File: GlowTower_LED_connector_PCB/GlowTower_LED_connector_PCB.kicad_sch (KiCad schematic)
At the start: 7 parts, among them SW1 TS-1102S-C-A-B, U1 LED strip, U2 LED strip, U3 LED strip, U4 LED strip, U5 SMTSO3015CTJ, U6 SMTSO3015CTJ

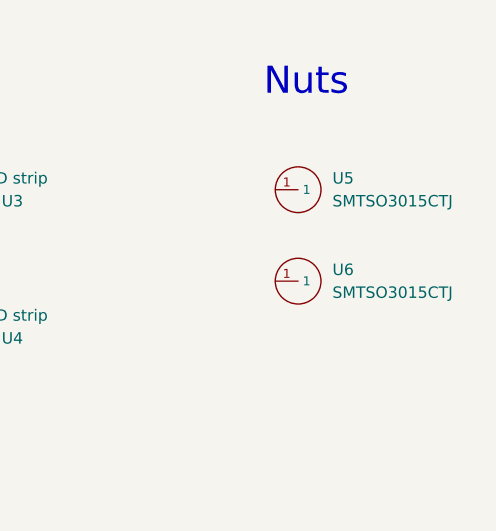
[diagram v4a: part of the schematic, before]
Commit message: improved connection to top case, added new glowtower design
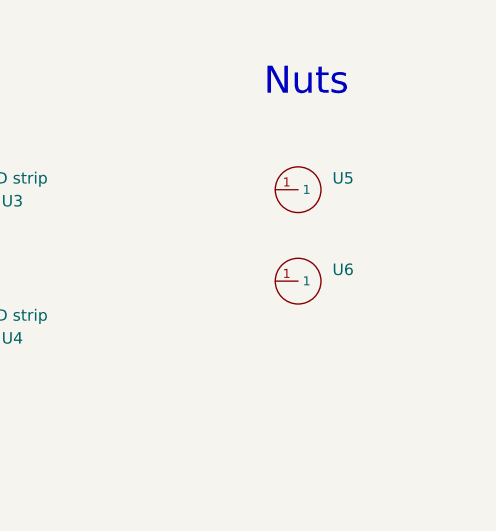
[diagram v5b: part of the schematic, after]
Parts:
- U5, U6: value SMTSO3015CTJ -> (none); footprint footprint:SMTSO3030CTJ -> (none); now left out of the parts list
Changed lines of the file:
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@@
   )
   (symbol (lib_id "MyParts:SMTSO3015CTJ") (at 116.84 39.37 0) (unit 1)
-    (in_bom yes) (on_board yes) (fields_autoplaced)
+    (in_bom no) (on_board yes) (fields_autoplaced)
     (property "Reference" "U6" (id 0) (at 120.65 44.4499 0)
       (effects (font (size 1.27 1.27)) (justify left))
     )
-    (property "Value" "SMTSO3015CTJ" (id 1) (at 120.65 46.9899 0)
+    (property "Value" "" (id 1) (at 120.65 46.9899 0)
       (effects (font (size 1.27 1.27)) (justify left))
     )
-    (property "Footprint" "footprint:SMTSO3030CTJ" (id 2) (at 116.84 49.53 0)
+    (property "Footprint" "" (id 2) (at 116.84 49.53 0)
       (effects (font (size 1.27 1.27) italic) hide)
     )
@@
   )
   (symbol (lib_id "MyParts:SMTSO3015CTJ") (at 116.84 29.21 0) (unit 1)
-    (in_bom yes) (on_board yes) (fields_autoplaced)
+    (in_bom no) (on_board yes) (fields_autoplaced)
     (property "Reference" "U5" (id 0) (at 120.65 34.2899 0)
       (effects (font (size 1.27 1.27)) (justify left))
     )
-    (property "Value" "SMTSO3015CTJ" (id 1) (at 120.65 36.8299 0)
+    (property "Value" "" (id 1) (at 120.65 36.8299 0)
       (effects (font (size 1.27 1.27)) (justify left))
     )
-    (property "Footprint" "footprint:SMTSO3030CTJ" (id 2) (at 116.84 39.37 0)
+    (property "Footprint" "" (id 2) (at 116.84 39.37 0)
       (effects (font (size 1.27 1.27) italic) hide)
     )
